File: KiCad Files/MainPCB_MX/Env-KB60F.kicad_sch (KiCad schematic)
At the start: 157 parts, among them J1 TP3 Pad, J2 TP2 Pad, SW1 EVQ-P7A01P, U1 Pico

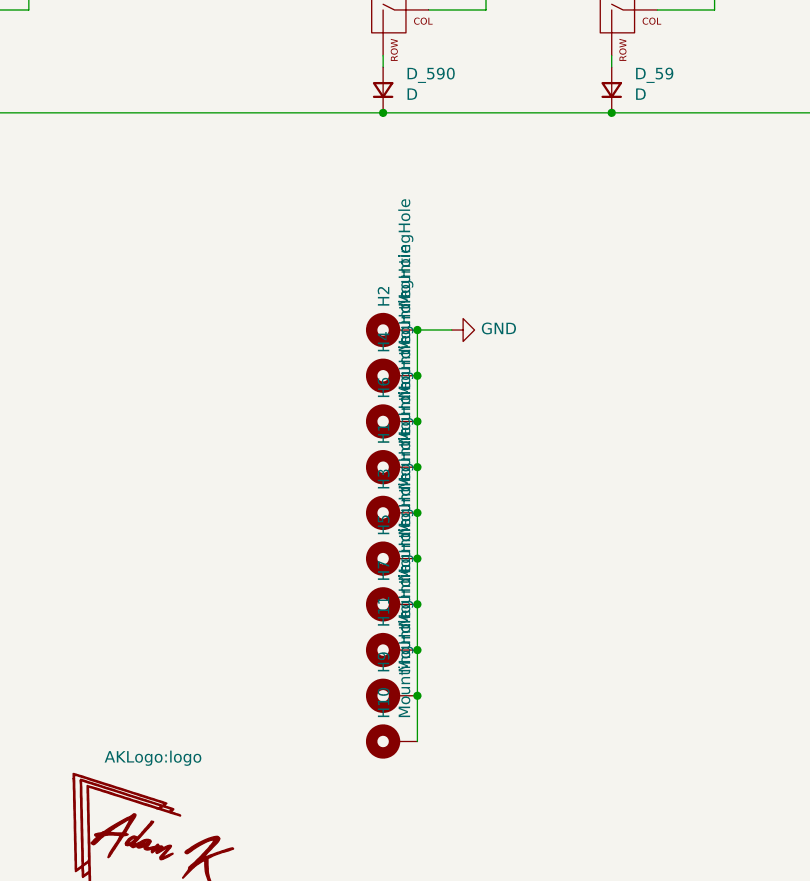
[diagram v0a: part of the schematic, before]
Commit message: made some temporary adjustments to test SMD Nuts
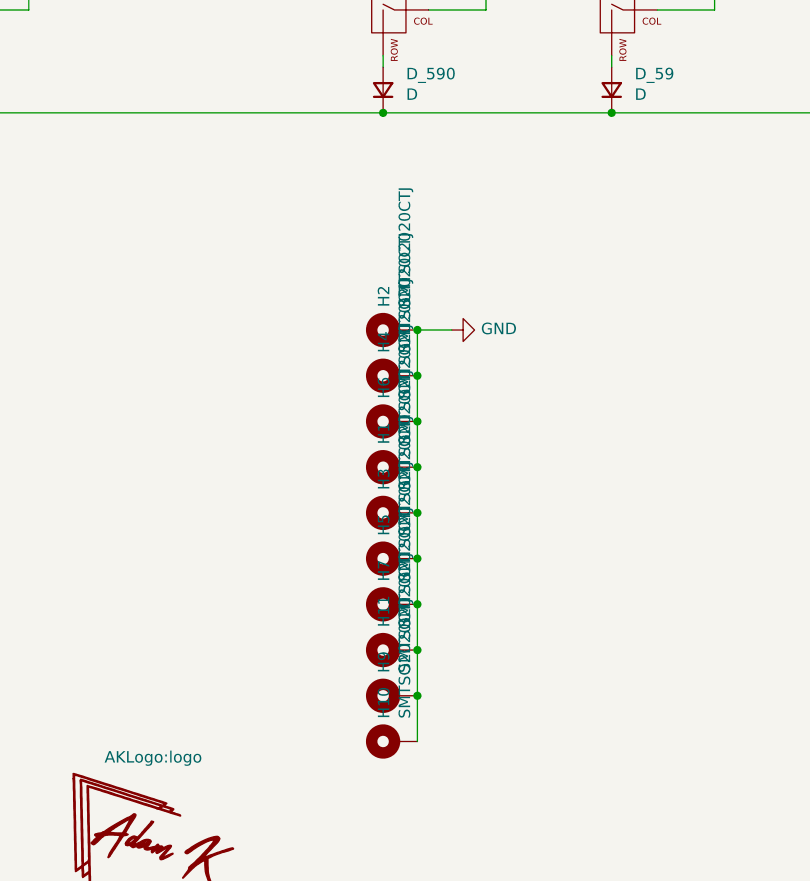
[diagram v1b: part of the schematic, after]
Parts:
- H1, H10, H11, H2, H3, H4, H5, H6, H7, H9: value MountingHole -> SMTSO2020CTJ
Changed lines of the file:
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@@
       (effects (font (size 1.27 1.27)) (justify left))
     )
-    (property "Value" "MountingHole" (id 1) (at 163.703 173.99 0)
+    (property "Value" "SMTSO2020CTJ" (id 1) (at 163.703 173.99 0)
       (effects (font (size 1.27 1.27)) (justify left))
     )
@@
       (effects (font (size 1.27 1.27)) (justify left))
     )
-    (property "Value" "MountingHole" (id 1) (at 163.703 179.07 0)
+    (property "Value" "SMTSO2020CTJ" (id 1) (at 163.703 179.07 0)
       (effects (font (size 1.27 1.27)) (justify left))
     )
@@
       (effects (font (size 1.27 1.27)) (justify left))
     )
-    (property "Value" "MountingHole" (id 1) (at 163.703 184.15 0)
+    (property "Value" "SMTSO2020CTJ" (id 1) (at 163.703 184.15 0)
       (effects (font (size 1.27 1.27)) (justify left))
     )
@@
       (effects (font (size 1.27 1.27)) (justify left))
     )
-    (property "Value" "MountingHole" (id 1) (at 163.703 189.23 0)
+    (property "Value" "SMTSO2020CTJ" (id 1) (at 163.703 189.23 0)
       (effects (font (size 1.27 1.27)) (justify left))
     )
@@
       (effects (font (size 1.27 1.27)) (justify left))
     )
-    (property "Value" "MountingHole" (id 1) (at 163.703 199.39 0)
+    (property "Value" "SMTSO2020CTJ" (id 1) (at 163.703 199.39 0)
       (effects (font (size 1.27 1.27)) (justify left))
     )
@@
       (effects (font (size 1.27 1.27)) (justify left))
     )
-    (property "Value" "MountingHole" (id 1) (at 163.703 204.47 0)
+    (property "Value" "SMTSO2020CTJ" (id 1) (at 163.703 204.47 0)
       (effects (font (size 1.27 1.27)) (justify left))
     )
@@
       (effects (font (size 1.27 1.27)) (justify left))
     )
-    (property "Value" "MountingHole" (id 1) (at 163.703 158.75 0)
+    (property "Value" "SMTSO2020CTJ" (id 1) (at 163.703 158.75 0)
       (effects (font (size 1.27 1.27)) (justify left))
     )
@@
       (effects (font (size 1.27 1.27)) (justify left))
     )
-    (property "Value" "MountingHole" (id 1) (at 163.703 163.83 0)
+    (property "Value" "SMTSO2020CTJ" (id 1) (at 163.703 163.83 0)
       (effects (font (size 1.27 1.27)) (justify left))
     )
@@
       (effects (font (size 1.27 1.27)) (justify left))
     )
-    (property "Value" "MountingHole" (id 1) (at 163.703 168.91 0)
+    (property "Value" "SMTSO2020CTJ" (id 1) (at 163.703 168.91 0)
       (effects (font (size 1.27 1.27)) (justify left))
     )
@@
       (effects (font (size 1.27 1.27)) (justify left))
     )
-    (property "Value" "MountingHole" (id 1) (at 163.703 194.31 0)
+    (property "Value" "SMTSO2020CTJ" (id 1) (at 163.703 194.31 0)
       (effects (font (size 1.27 1.27)) (justify left))
     )
@@
     )
     (path "/00000000-0000-0000-0000-0000608ab119"
-      (reference "H1") (unit 1) (value "MountingHole") (footprint "Env_Extras:MountingHole_2.2mm_M2-MODIFIED")
+      (reference "H1") (unit 1) (value "SMTSO2020CTJ") (footprint "Env_Extras:MountingHole_2.2mm_M2-MODIFIED")
     )
     (path "/00000000-0000-0000-0000-0000609389ef"
-      (reference "H2") (unit 1) (value "MountingHole") (footprint "Env_Extras:MountingHole_2.2mm_M2-MODIFIED")
+      (reference "H2") (unit 1) (value "SMTSO2020CTJ") (footprint "Env_Extras:MountingHole_2.2mm_M2-MODIFIED")
     )
     (path "/00000000-0000-0000-0000-0000608acb73"
-      (reference "H3") (unit 1) (value "MountingHole") (footprint "Env_Extras:MountingHole_2.2mm_M2-MODIFIED")
+      (reference "H3") (unit 1) (value "SMTSO2020CTJ") (footprint "Env_Extras:MountingHole_2.2mm_M2-MODIFIED")
     )
     (path "/00000000-0000-0000-0000-0000609389f5"
-      (reference "H4") (unit 1) (value "MountingHole") (footprint "Env_Extras:MountingHole_2.2mm_M2-MODIFIED")
+      (reference "H4") (unit 1) (value "SMTSO2020CTJ") (footprint "Env_Extras:MountingHole_2.2mm_M2-MODIFIED")
     )
     (path "/00000000-0000-0000-0000-0000608bcf9c"
-      (reference "H5") (unit 1) (value "MountingHole") (footprint "Env_Extras:MountingHole_2.2mm_M2-MODIFIED")
+      (reference "H5") (unit 1) (value "SMTSO2020CTJ") (footprint "Env_Extras:MountingHole_2.2mm_M2-MODIFIED")
     )
     (path "/00000000-0000-0000-0000-0000609389fb"
-      (reference "H6") (unit 1) (value "MountingHole") (footprint "Env_Extras:MountingHole_2.2mm_M2-MODIFIED")
+      (reference "H6") (unit 1) (value "SMTSO2020CTJ") (footprint "Env_Extras:MountingHole_2.2mm_M2-MODIFIED")
     )
     (path "/00000000-0000-0000-0000-0000608cd285"
-      (reference "H7") (unit 1) (value "MountingHole") (footprint "Env_Extras:MountingHole_2.2mm_M2-MODIFIED")
+      (reference "H7") (unit 1) (value "SMTSO2020CTJ") (footprint "Env_Extras:MountingHole_2.2mm_M2-MODIFIED")
     )
     (path "/00000000-0000-0000-0000-0000608dd691"
-      (reference "H9") (unit 1) (value "MountingHole") (footprint "Env_Extras:MountingHole_2.2mm_M2-MODIFIED")
+      (reference "H9") (unit 1) (value "SMTSO2020CTJ") (footprint "Env_Extras:MountingHole_2.2mm_M2-MODIFIED")
     )
     (path "/00000000-0000-0000-0000-0000608edb63"
-      (reference "H10") (unit 1) (value "MountingHole") (footprint "Env_Extras:MountingHole_2.2mm_M2-MODIFIED")
+      (reference "H10") (unit 1) (value "SMTSO2020CTJ") (footprint "Env_Extras:MountingHole_2.2mm_M2-MODIFIED")
     )
     (path "/00000000-0000-0000-0000-0000609431fd"
-      (reference "H11") (unit 1) (value "MountingHole") (footprint "Env_Extras:MountingHole_2.2mm_M2-MODIFIED")
+      (reference "H11") (unit 1) (value "SMTSO2020CTJ") (footprint "Env_Extras:MountingHole_2.2mm_M2-MODIFIED")
     )
     (path "/00000000-0000-0000-0000-000060b4329c"

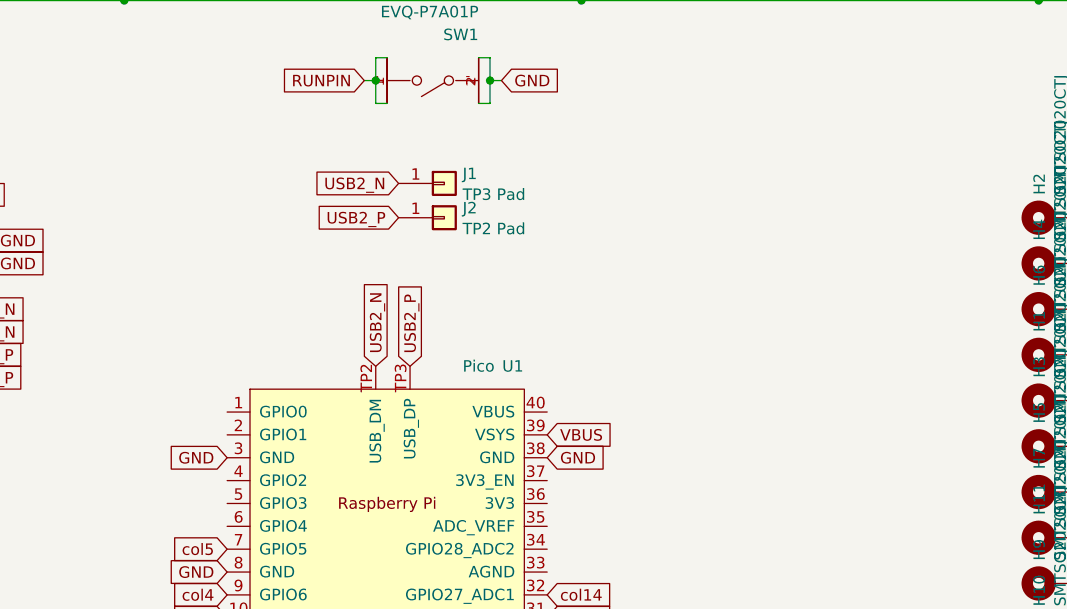
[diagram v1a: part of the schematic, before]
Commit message: added I2C header and protection diode to MX version
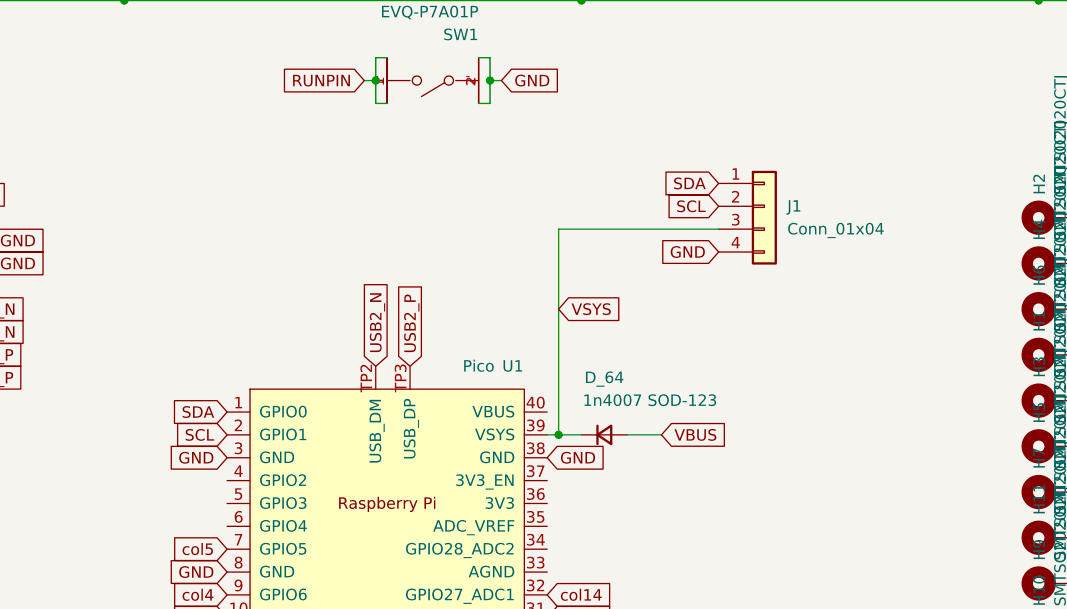
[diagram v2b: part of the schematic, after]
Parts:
- removed J1: TP3 Pad, TestPoint:TestPoint_Pad_1.0x1.0mm, symbol Connector_Generic:Conn_01x01
- removed J2: TP2 Pad, TestPoint:TestPoint_Pad_1.0x1.0mm, symbol Connector_Generic:Conn_01x01
- added D_64: 1n4007 SOD-123, Diode_SMD:D_SOD-123, symbol Device:D_Small
- added J1: Conn_01x04, Connector_PinSocket_2.54mm:PinSocket_1x04_P2.54mm_Vertical, symbol Connector_Generic:Conn_01x04
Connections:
- net GND: now also J1.4 (Pin_4)
- net VBUS: now also D_64.2 (A); no longer U1.39 (VSYS)
- net SDA: now reaches U1.1 (GPIO0)
- net SDA: now also J1.1 (Pin_1)
- net SCL: now reaches U1.2 (GPIO1)
- net SCL: now also J1.2 (Pin_2)
- new net VSYS: D_64.1 (K), J1.3 (Pin_3), U1.39 (VSYS)
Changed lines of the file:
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@@
   (junction (at 121.92 24.13) (diameter 0) (color 0 0 0 0)
   )
+  (junction (at 107.95 185.42) (diameter 0) (color 0 0 0 0)
+  )
   (junction (at 59.69 35.56) (diameter 0) (color 0 0 0 0)
   )
@@
     (stroke (width 0) (type default) (color 0 0 0 0))
   )
+  (wire (pts (xy 107.95 162.56) (xy 107.95 185.42))
+    (stroke (width 0) (type default) (color 0 0 0 0))
+  )
   (wire (pts (xy 325.12 74.93) (xy 325.12 49.53))
     (stroke (width 0) (type default) (color 0 0 0 0))
@@
     (stroke (width 0) (type default) (color 0 0 0 0))
   )
+  (wire (pts (xy 107.95 185.42) (xy 106.68 185.42))
+    (stroke (width 0) (type default) (color 0 0 0 0))
+  )
   (wire (pts (xy 242.57 24.13) (xy 248.92 24.13))
     (stroke (width 0) (type default) (color 0 0 0 0))
@@
     (stroke (width 0) (type default) (color 0 0 0 0))
   )
+  (wire (pts (xy 125.73 162.56) (xy 107.95 162.56))
+    (stroke (width 0) (type default) (color 0 0 0 0))
+  )
   (wire (pts (xy 212.09 80.01) (xy 212.09 81.28))
     (stroke (width 0) (type default) (color 0 0 0 0))
@@
     (stroke (width 0) (type default) (color 0 0 0 0))
   )
+  (wire (pts (xy 110.49 185.42) (xy 107.95 185.42))
+    (stroke (width 0) (type default) (color 0 0 0 0))
+  )
   (wire (pts (xy 237.49 60.96) (xy 262.89 60.96))
     (stroke (width 0) (type default) (color 0 0 0 0))
@@
     (stroke (width 0) (type default) (color 0 0 0 0))
   )
+  (wire (pts (xy 119.38 185.42) (xy 115.57 185.42))
+    (stroke (width 0) (type default) (color 0 0 0 0))
+  )
   (wire (pts (xy 401.32 125.73) (xy 401.32 74.93))
     (stroke (width 0) (type default) (color 0 0 0 0))
@@
     )
   )
+  (global_label "SDA" (shape input) (at 71.12 182.88 180) (fields_autoplaced)
+    (effects (font (size 1.27 1.27)) (justify right))
+    (property "Intersheet References" "${INTERSHEET_REFS}" (id 0) (at 65.2277 182.8006 0)
+      (effects (font (size 1.27 1.27)) (justify right) hide)
+    )
+  )
   (global_label "col12" (shape input) (at 106.68 210.82 0) (fields_autoplaced)
     (effects (font (size 1.27 1.27)) (justify left))
@@
     )
   )
+  (global_label "GND" (shape input) (at 125.73 165.1 180) (fields_autoplaced)
+    (effects (font (size 1.27 1.27)) (justify right))
+    (property "Intersheet References" "${INTERSHEET_REFS}" (id 0) (at 232.41 353.06 0)
+      (effects (font (size 1.27 1.27)) hide)
+    )
+  )
   (global_label "USB2_P" (shape input) (at 39.37 179.07 0) (fields_autoplaced)
     (effects (font (size 1.27 1.27)) (justify left))
@@
     )
   )
+  (global_label "VSYS" (shape input) (at 107.95 171.45 0) (fields_autoplaced)
+    (effects (font (size 1.27 1.27)) (justify left))
+    (property "Intersheet References" "${INTERSHEET_REFS}" (id 0) (at 114.8704 171.3706 0)
+      (effects (font (size 1.27 1.27)) (justify left) hide)
+    )
+  )
   (global_label "GND" (shape input) (at 44.45 163.83 0) (fields_autoplaced)
     (effects (font (size 1.27 1.27)) (justify left))
@@
     )
   )
+  (global_label "SDA" (shape input) (at 125.73 157.48 180) (fields_autoplaced)
+    (effects (font (size 1.27 1.27)) (justify right))
+    (property "Intersheet References" "${INTERSHEET_REFS}" (id 0) (at 119.8377 157.4006 0)
+      (effects (font (size 1.27 1.27)) (justify right) hide)
+    )
+  )
   (global_label "col12" (shape input) (at 350.52 16.51 180) (fields_autoplaced)
     (effects (font (size 1.27 1.27)) (justify right))
@@
     )
   )
+  (global_label "SCL" (shape input) (at 125.73 160.02 180) (fields_autoplaced)
+    (effects (font (size 1.27 1.27)) (justify right))
+    (property "Intersheet References" "${INTERSHEET_REFS}" (id 0) (at 119.8982 159.9406 0)
+      (effects (font (size 1.27 1.27)) (justify right) hide)
+    )
+  )
   (global_label "GND" (shape input) (at 106.68 213.36 0) (fields_autoplaced)
     (effects (font (size 1.27 1.27)) (justify left))
@@
     )
   )
-  (global_label "USB2_P" (shape input) (at 90.17 161.29 180) (fields_autoplaced)
-    (effects (font (size 1.27 1.27)) (justify right))
-    (property "Intersheet References" "${INTERSHEET_REFS}" (id 0) (at 0 0 0)
-      (effects (font (size 1.27 1.27)) hide)
-    )
-  )
   (global_label "GND" (shape input) (at 71.12 213.36 180) (fields_autoplaced)
     (effects (font (size 1.27 1.27)) (justify right))
@@
     )
   )
-  (global_label "USB2_N" (shape input) (at 90.17 157.48 180) (fields_autoplaced)
-    (effects (font (size 1.27 1.27)) (justify right))
-    (property "Intersheet References" "${INTERSHEET_REFS}" (id 0) (at 0 0 0)
-      (effects (font (size 1.27 1.27)) hide)
-    )
-  )
   (global_label "col5" (shape input) (at 71.12 198.12 180) (fields_autoplaced)
     (effects (font (size 1.27 1.27)) (justify right))
@@
     )
   )
+  (global_label "SCL" (shape input) (at 71.12 185.42 180) (fields_autoplaced)
+    (effects (font (size 1.27 1.27)) (justify right))
+    (property "Intersheet References" "${INTERSHEET_REFS}" (id 0) (at 65.2882 185.3406 0)
+      (effects (font (size 1.27 1.27)) (justify right) hide)
+    )
+  )
   (global_label "row1" (shape input) (at 22.86 60.96 180) (fields_autoplaced)
     (effects (font (size 1.27 1.27)) (justify right))
@@
     )
   )
-  (global_label "VBUS" (shape input) (at 106.68 185.42 0) (fields_autoplaced)
+  (global_label "VBUS" (shape input) (at 119.38 185.42 0) (fields_autoplaced)
     (effects (font (size 1.27 1.27)) (justify left))
-    (property "Intersheet References" "${INTERSHEET_REFS}" (id 0) (at 0 2.54 0)
+    (property "Intersheet References" "${INTERSHEET_REFS}" (id 0) (at 12.7 2.54 0)
       (effects (font (size 1.27 1.27)) hide)
     )
@@
     (pin "2")
   )
-  (symbol (lib_id "Connector_Generic:Conn_01x01") (at 95.25 157.48 0) (unit 1)
-    (in_bom yes) (on_board yes)
-    (property "Reference" "J1" (id 0) (at 97.282 156.4132 0)
-      (effects (font (size 1.27 1.27)) (justify left))
-    )
-    (property "Value" "TP3 Pad" (id 1) (at 97.282 158.7246 0)
-      (effects (font (size 1.27 1.27)) (justify left))
-    )
-    (property "Footprint" "TestPoint:TestPoint_Pad_1.0x1.0mm" (id 2) (at 95.25 157.48 0)
-      (effects (font (size 1.27 1.27)) hide)
-    )
-    (property "Datasheet" "~" (id 3) (at 95.25 157.48 0)
-      (effects (font (size 1.27 1.27)) hide)
-    )
-    (pin "1")
-  )
-  (symbol (lib_id "Connector_Generic:Conn_01x01") (at 95.25 161.29 0) (unit 1)
-    (in_bom yes) (on_board yes)
-    (property "Reference" "J2" (id 0) (at 97.282 160.2232 0)
-      (effects (font (size 1.27 1.27)) (justify left))
-    )
-    (property "Value" "TP2 Pad" (id 1) (at 97.282 162.5346 0)
-      (effects (font (size 1.27 1.27)) (justify left))
-    )
-    (property "Footprint" "TestPoint:TestPoint_Pad_1.0x1.0mm" (id 2) (at 95.25 161.29 0)
-      (effects (font (size 1.27 1.27)) hide)
-    )
-    (property "Datasheet" "~" (id 3) (at 95.25 161.29 0)
-      (effects (font (size 1.27 1.27)) hide)
-    )
-    (pin "1")
-  )
   (symbol (lib_id "Device:D_Small") (at 161.29 134.62 90) (unit 1)
     (in_bom yes) (on_board yes)
@@
     (pin "2")
   )
+  (symbol (lib_id "Device:D_Small") (at 113.03 185.42 0) (unit 1)
+    (in_bom yes) (on_board yes)
+    (property "Reference" "D_64" (id 0) (at 113.03 179.07 0))
+    (property "Value" "1n4007 SOD-123" (id 1) (at 118.11 181.61 0))
+    (property "Footprint" "Diode_SMD:D_SOD-123" (id 2) (at 113.03 185.42 90)
+      (effects (font (size 1.27 1.27)) hide)
+    )
+    (property "Datasheet" "~" (id 3) (at 113.03 185.42 90)
+      (effects (font (size 1.27 1.27)) hide)
+    )
+    (pin "1")
+    (pin "2")
+  )
+  (symbol (lib_id "Connector_Generic:Conn_01x04") (at 130.81 160.02 0) (unit 1)
+    (in_bom yes) (on_board yes) (fields_autoplaced)
+    (property "Reference" "J1" (id 0) (at 133.35 160.0199 0)
+      (effects (font (size 1.27 1.27)) (justify left))
+    )
+    (property "Value" "Conn_01x04" (id 1) (at 133.35 162.5599 0)
+      (effects (font (size 1.27 1.27)) (justify left))
+    )
+    (property "Footprint" "Connector_PinSocket_2.54mm:PinSocket_1x04_P2.54mm_Vertical" (id 2) (at 130.81 160.02 0)
+      (effects (font (size 1.27 1.27)) hide)
+    )
+    (property "Datasheet" "~" (id 3) (at 130.81 160.02 0)
+      (effects (font (size 1.27 1.27)) hide)
+    )
+    (pin "1")
+    (pin "2")
+    (pin "3")
+    (pin "4")
+  )
   (symbol (lib_id "Mechanical:MountingHole") (at 166.37 229.235 0) (unit 1)
     (in_bom yes) (on_board yes)
@@
       (reference "D_63") (unit 1) (value "D") (footprint "Diode_THT:D_DO-35_SOD27_P7.62mm_Horizontal")
     )
+    (path "/9c589f50-4ac7-4470-b638-e29a11f3fc3c"
+      (reference "D_64") (unit 1) (value "1n4007 SOD-123") (footprint "Diode_SMD:D_SOD-123")
+    )
     (path "/00000000-0000-0000-0000-0000612e0015"
       (reference "D_590") (unit 1) (value "D") (footprint "Diode_THT:D_DO-35_SOD27_P7.62mm_Horizontal")
@@
       (reference "H11") (unit 1) (value "SMTSO2020CTJ") (footprint "Env_Extras:MountingHole_2.2mm_M2-MODIFIED")
     )
-    (path "/00000000-0000-0000-0000-000060b4329c"
-      (reference "J1") (unit 1) (value "TP3 Pad") (footprint "TestPoint:TestPoint_Pad_1.0x1.0mm")
-    )
-    (path "/00000000-0000-0000-0000-000060b44b24"
-      (reference "J2") (unit 1) (value "TP2 Pad") (footprint "TestPoint:TestPoint_Pad_1.0x1.0mm")
+    (path "/ad188452-862f-4110-adcf-92ca74aeb0da"
+      (reference "J1") (unit 1) (value "Conn_01x04") (footprint "Connector_PinSocket_2.54mm:PinSocket_1x04_P2.54mm_Vertical")
     )
     (path "/00000000-0000-0000-0000-000000000001"
